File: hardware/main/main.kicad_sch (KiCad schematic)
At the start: 22 parts, among them J101 ST_LINK, J102 USART

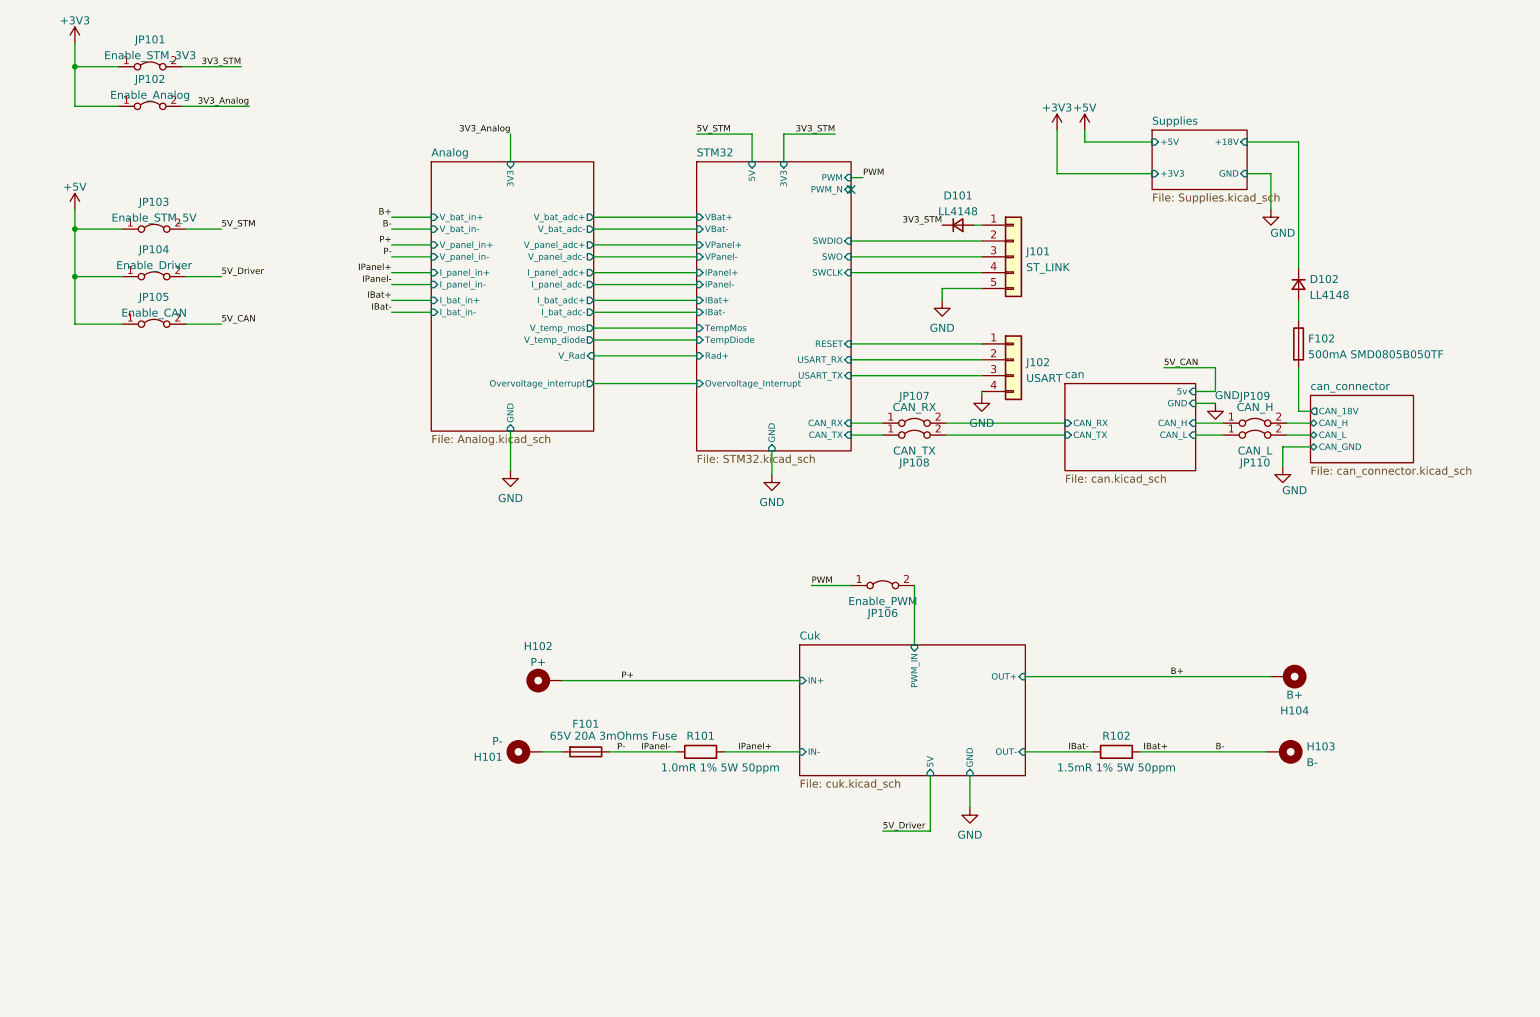
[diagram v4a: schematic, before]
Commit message: Layout: Organizing components
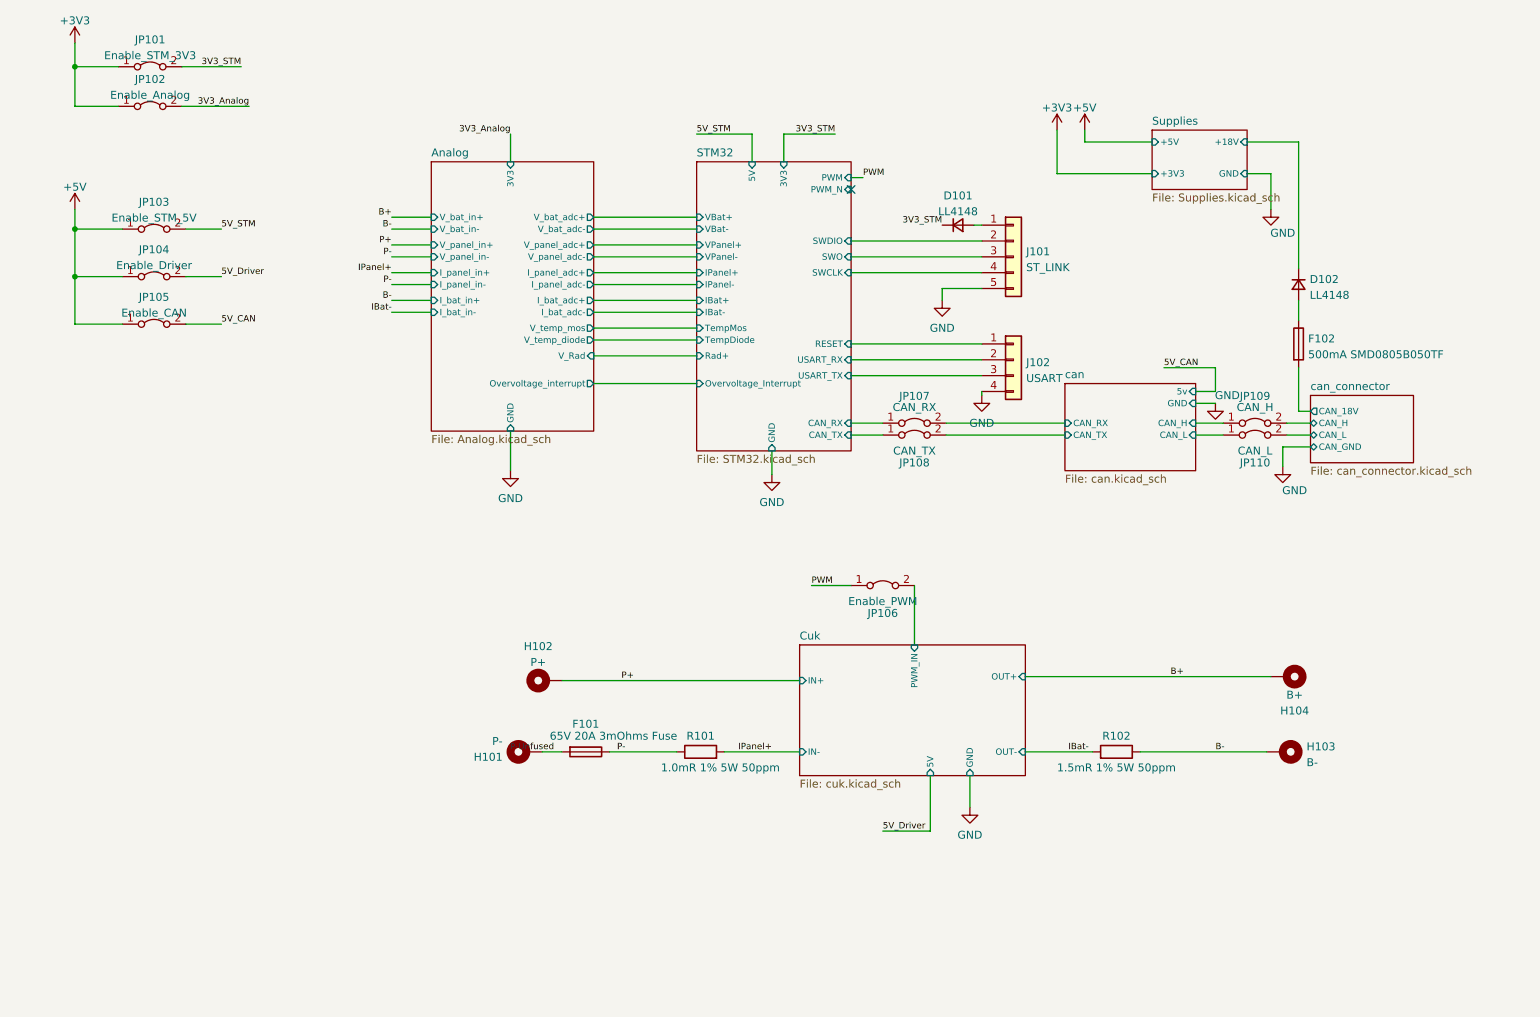
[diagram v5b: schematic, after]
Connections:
- net P-Unfused: now reaches F101.2, H101.1
- net IPanel- renamed P-
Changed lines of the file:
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@@
     (effects (font (size 1.016 1.016)) (justify left bottom))
-  )
-  (label "IBat+" (at 82.55 66.675 180)
-    (effects (font (size 1.016 1.016)) (justify right bottom))
   )
   (label "PWM" (at 158.115 46.99 0)
@@
     (effects (font (size 1.016 1.016)) (justify left bottom))
   )
-  (label "IPanel-" (at 122.555 139.065 0)
-    (effects (font (size 1.016 1.016)) (justify left bottom))
-  )
   (label "5V_STM" (at 131.445 40.005 0)
     (effects (font (size 1.016 1.016)) (justify left bottom))
   )
-  (label "IBat+" (at 207.01 139.065 180)
-    (effects (font (size 1.016 1.016)) (justify right bottom))
-  )
-  (label "IPanel-" (at 82.55 64.135 180)
+  (label "B-" (at 82.55 66.675 180)
     (effects (font (size 1.016 1.016)) (justify right bottom))
   )
@@
     (effects (font (size 1.016 1.016)) (justify right bottom))
   )
+  (label "P-Unfused" (at 108.585 139.065 180)
+    (effects (font (size 1.016 1.016)) (justify right bottom))
+  )
   (label "3V3_Analog" (at 59.69 35.56 180)
+    (effects (font (size 1.016 1.016)) (justify right bottom))
+  )
+  (label "P-" (at 82.55 64.135 180)
     (effects (font (size 1.016 1.016)) (justify right bottom))
   )
@@
     )
     (path "/5ce5fb2d-189a-4c71-a5ce-76d878c8bc18/13178051-ce3b-44a3-a4b5-07bdcc08ab27"
-      (reference "U301") (unit 1) (value "INA823DT") (footprint "Package_SO:VSSOP-8_3.0x3.0mm_P0.65mm")
+      (reference "U301") (unit 1) (value "INA823DT") (footprint "Package_SO:SOIC-8_3.9x4.9mm_P1.27mm")
     )
     (path "/5ce5fb2d-189a-4c71-a5ce-76d878c8bc18/0f96a9a7-6e14-4762-a8f5-64e8fe1e058f"
-      (reference "U302") (unit 1) (value "INA823DT") (footprint "Package_SO:VSSOP-8_3.0x3.0mm_P0.65mm")
+      (reference "U302") (unit 1) (value "INA823DT") (footprint "Package_SO:SOIC-8_3.9x4.9mm_P1.27mm")
     )
     (path "/5ce5fb2d-189a-4c71-a5ce-76d878c8bc18/88af16c3-9e23-4dbf-ae59-73b8c6015226"
@@
     )
     (path "/5ce5fb2d-189a-4c71-a5ce-76d878c8bc18/bf66e27a-ba1e-4d27-92c8-c354c9c40cf8"
-      (reference "U305") (unit 1) (value "TL7726IDR_1") (footprint "Package_SON:X2SON-8_1.4x1mm_P0.35mm")
+      (reference "U305") (unit 1) (value "TL7726IDR_1") (footprint "Package_SO:SOIC-8_3.9x4.9mm_P1.27mm")
     )
     (path "/9e3280d3-dce3-416e-a0bb-0596067104fa/cc3e596f-ddde-41c2-a2e5-ac6a660b9c6c/27d72f4b-3bcb-48dc-9ea4-d43f85bfdfe8"
       (reference "U501") (unit 1) (value "1EDI60N12AF") (footprint "Package_SO:SOIC-8_3.9x4.9mm_P1.27mm")
     )
-    (path "/928491fe-3bfe-4b2d-9fd0-bf4405232f71/fa904ab6-fc50-4b7e-9768-7e2dcbaf9da9"
+    (path "/928491fe-3bfe-4b2d-9fd0-bf4405232f71/45b34e39-8a86-4ca9-a65a-5ab8d5890b57"
       (reference "U601") (unit 1) (value "VXO7805-1000") (footprint "Zenite:TO-220-3_Horizontal_TabDown_SMD")
     )

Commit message: Layout: Organizing power components
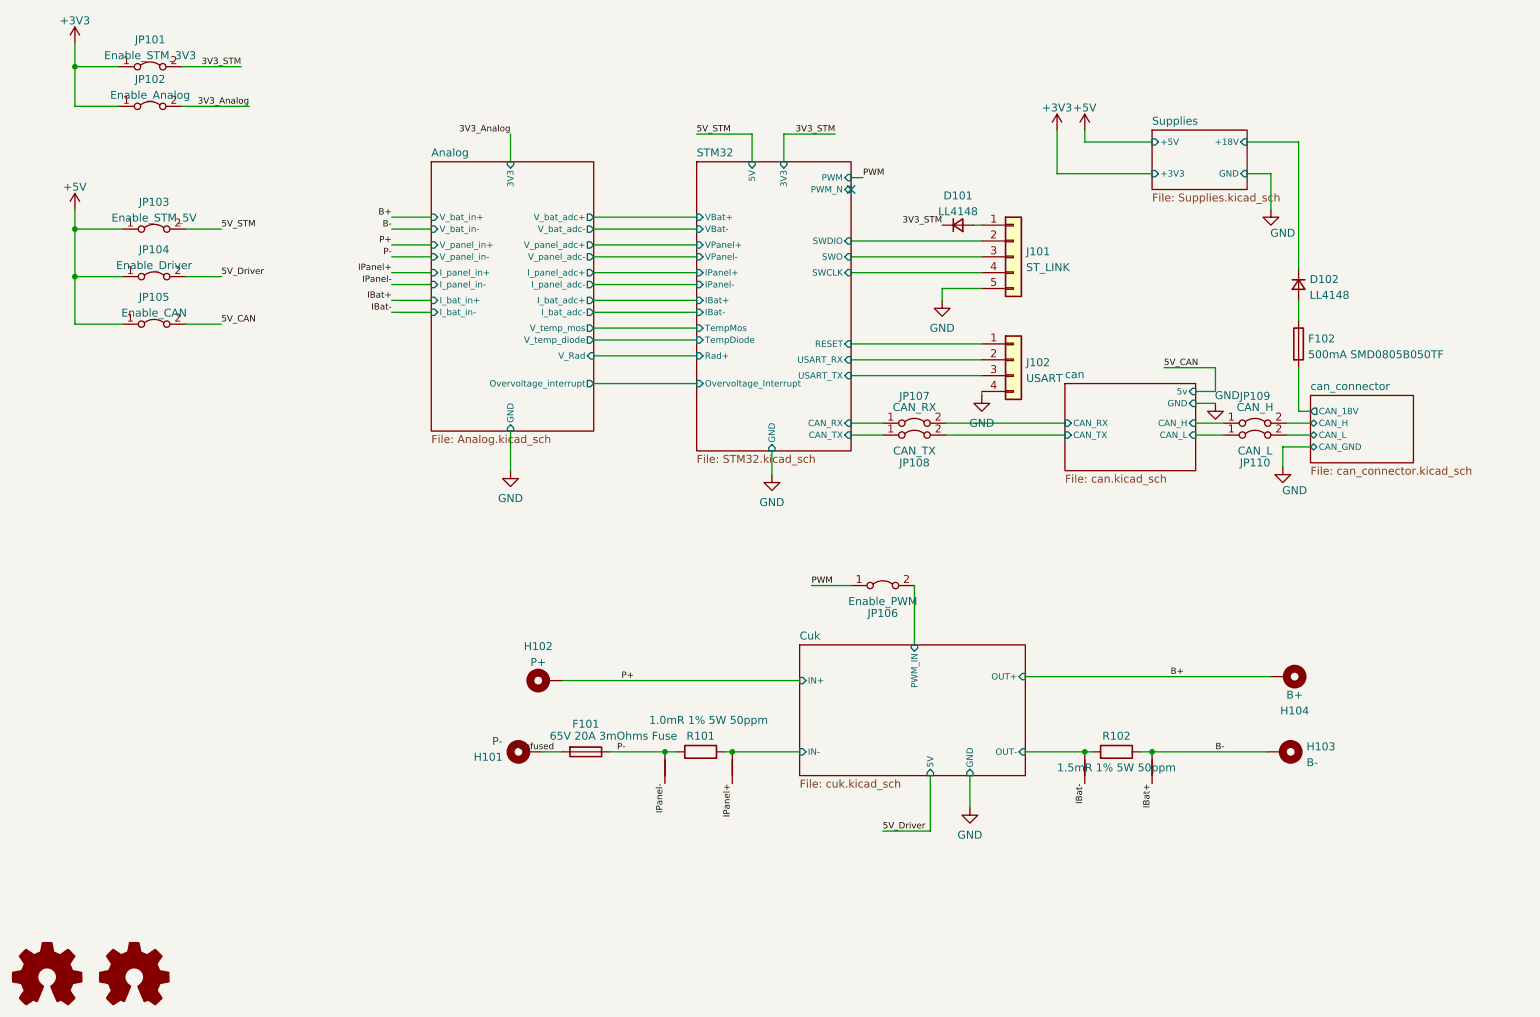
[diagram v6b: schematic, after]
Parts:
- added LOGO101: Logo_Open_Hardware_Small, Zenite:symbol_logoZenite, symbol Graphic:Logo_Open_Hardware_Small
- added LOGO102: Logo_Open_Hardware_Small, Zenite:synbol_logoifsc, symbol Graphic:Logo_Open_Hardware_Small
- added NT101, NT102, NT104: NetTie_2, Resistor_SMD:R_0201_0603Metric, symbol Device:NetTie_2
- added NT103: Resistor_SMD:R_0201_0603Metric, Resistor_SMD:R_0201_0603Metric, symbol Device:NetTie_2
- H101, H102, H103, H104: footprint Zenite:MountingHole_12mmx12mm_Rectangular -> Zenite:MountingHole_13mmx13mm_Rectangular
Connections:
- net B-: now also NT104.2
- net IBat-: now also NT103.1; no longer R102.2
- net IPanel+: now also NT102.1; no longer R101.2
- net P-: now also NT101.2
- new net Cuk/IN-: NT102.2, R101.2
- new net Cuk/OUT-: NT103.2, R102.2
- new net IBat+: NT104.1
- new net IPanel-: NT101.1
